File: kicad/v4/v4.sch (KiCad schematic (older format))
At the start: 31 parts, among them J1 BNC, J1-1 Head1_1, J1-2 Head1_1, J2 BNC, J2-1 Head1_1, J2-2 Head1_1, J2-3 Head1_1, J3 Red, J3-1 Head1_1, J3-2 Head1_1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

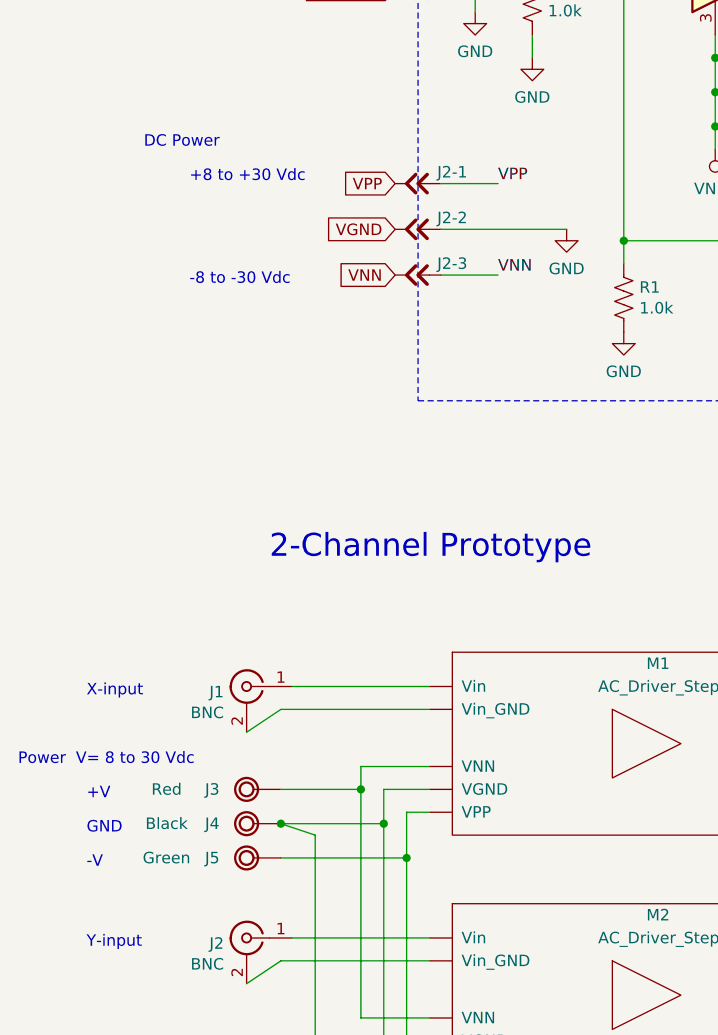
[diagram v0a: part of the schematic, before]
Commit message: Schematic:  Rename (reorder) power terminals to match the "as-built" board,     putting the negative supply first.
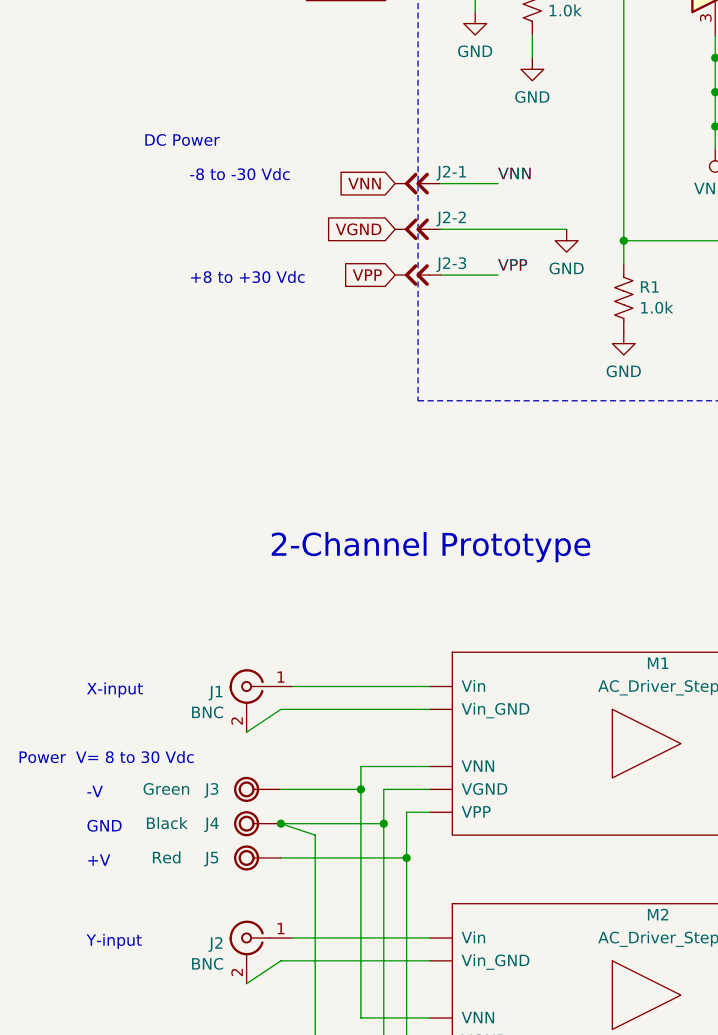
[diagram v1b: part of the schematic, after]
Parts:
- J3: value Red -> Green
- J5: value Green -> Red
- renumbered J2-3 to J2-1, J2-1 to J2-3
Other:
- moved on the sheet: J2-1, J2-3
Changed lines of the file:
@@
 Text Notes 7850 2900 0    50   ~ 0
 1:11.8
-Text GLabel 2200 3150 0    50   Input ~ 0
+Text GLabel 2200 3550 0    50   Input ~ 0
 VPP
 Text GLabel 2200 3350 0    50   Input ~ 0
 VGND
-Text GLabel 2200 3550 0    50   Input ~ 0
+Text GLabel 2200 3150 0    50   Input ~ 0
 VNN
+Text Notes 1300 3600 0    50   ~ 0
++8 to +30 Vdc
 Text Notes 1300 3150 0    50   ~ 0
-+8 to +30 Vdc
-Text Notes 1300 3600 0    50   ~ 0
 -8 to -30 Vdc
 $Comp
@@
 P 1550 5800
 F 0 "J3" H 1400 5800 50  0000 C CNN
-F 1 "Red" H 1200 5800 50  0000 C CNN
+F 1 "Green" H 1200 5800 50  0000 C CNN
 F 2 "" H 1550 5800 50  0001 C CNN
 F 3 "" H 1550 5800 50  0001 C CNN
@@
 P 1550 6100
 F 0 "J5" H 1400 6100 50  0000 C CNN
-F 1 "Green" H 1200 6100 50  0000 C CNN
+F 1 "Red" H 1200 6100 50  0000 C CNN
 F 2 "" H 1550 6100 50  0001 C CNN
 F 3 "" H 1550 6100 50  0001 C CNN
@@
 	2400 3350 2950 3350
 $Comp
+L _Local:Head1_1 J2-3
+U 1 1 5C40469D
+P 2300 3550
+F 0 "J2-3" H 2150 3600 50  0000 C CNN
+F 1 "Head1_1" H 2300 3350 50  0001 C CNN
+F 2 "" H 2300 3550 50  0001 C CNN
+F 3 "" H 2300 3550 50  0001 C CNN
+	1    2300 3550
+	-1   0    0    -1
+$EndComp
+$Comp
 L _Local:Head1_1 J2-1
-U 1 1 5C40469D
+U 1 1 5C4046F5
 P 2300 3150
 F 0 "J2-1" H 2150 3200 50  0000 C CNN
@@
 	-1   0    0    -1
 $EndComp
-$Comp
-L _Local:Head1_1 J2-3
-U 1 1 5C4046F5
-P 2300 3550
-F 0 "J2-3" H 2150 3600 50  0000 C CNN
-F 1 "Head1_1" H 2300 3350 50  0001 C CNN
-F 2 "" H 2300 3550 50  0001 C CNN
-F 3 "" H 2300 3550 50  0001 C CNN
-	1    2300 3550
-	-1   0    0    -1
-$EndComp
+Text Label 2650 3550 0    50   ~ 0
+VPP
+Wire Wire Line
+	2400 3550 2650 3550
+Wire Wire Line
+	2400 3150 2650 3150
 Text Label 2650 3150 0    50   ~ 0
-VPP
-Wire Wire Line
-	2400 3150 2650 3150
-Wire Wire Line
-	2400 3550 2650 3550
-Text Label 2650 3550 0    50   ~ 0
 VNN
 $Comp
@@
 Y-input
 Text Notes 850  5850 0    50   ~ 0
+-V
+Text Notes 850  6150 0    50   ~ 0
 +V
-Text Notes 850  6150 0    50   ~ 0
--V
 Text Notes 850  6000 0    50   ~ 0
 GND

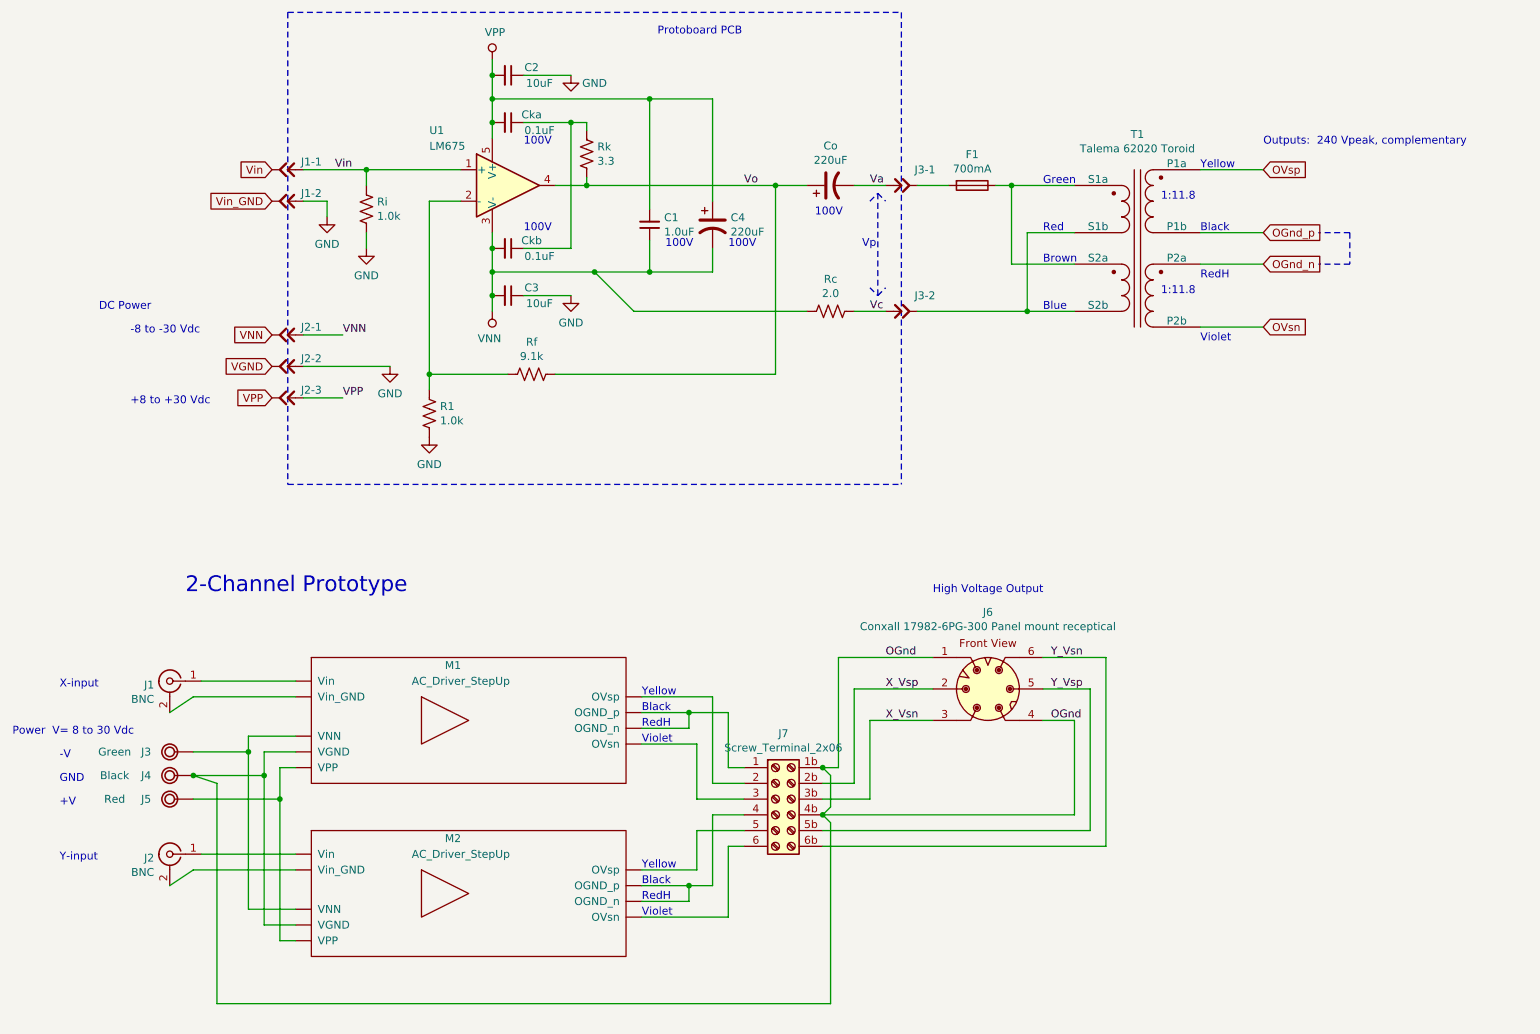
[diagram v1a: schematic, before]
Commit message: Schematic:  Add input/output notes and transformer rating.
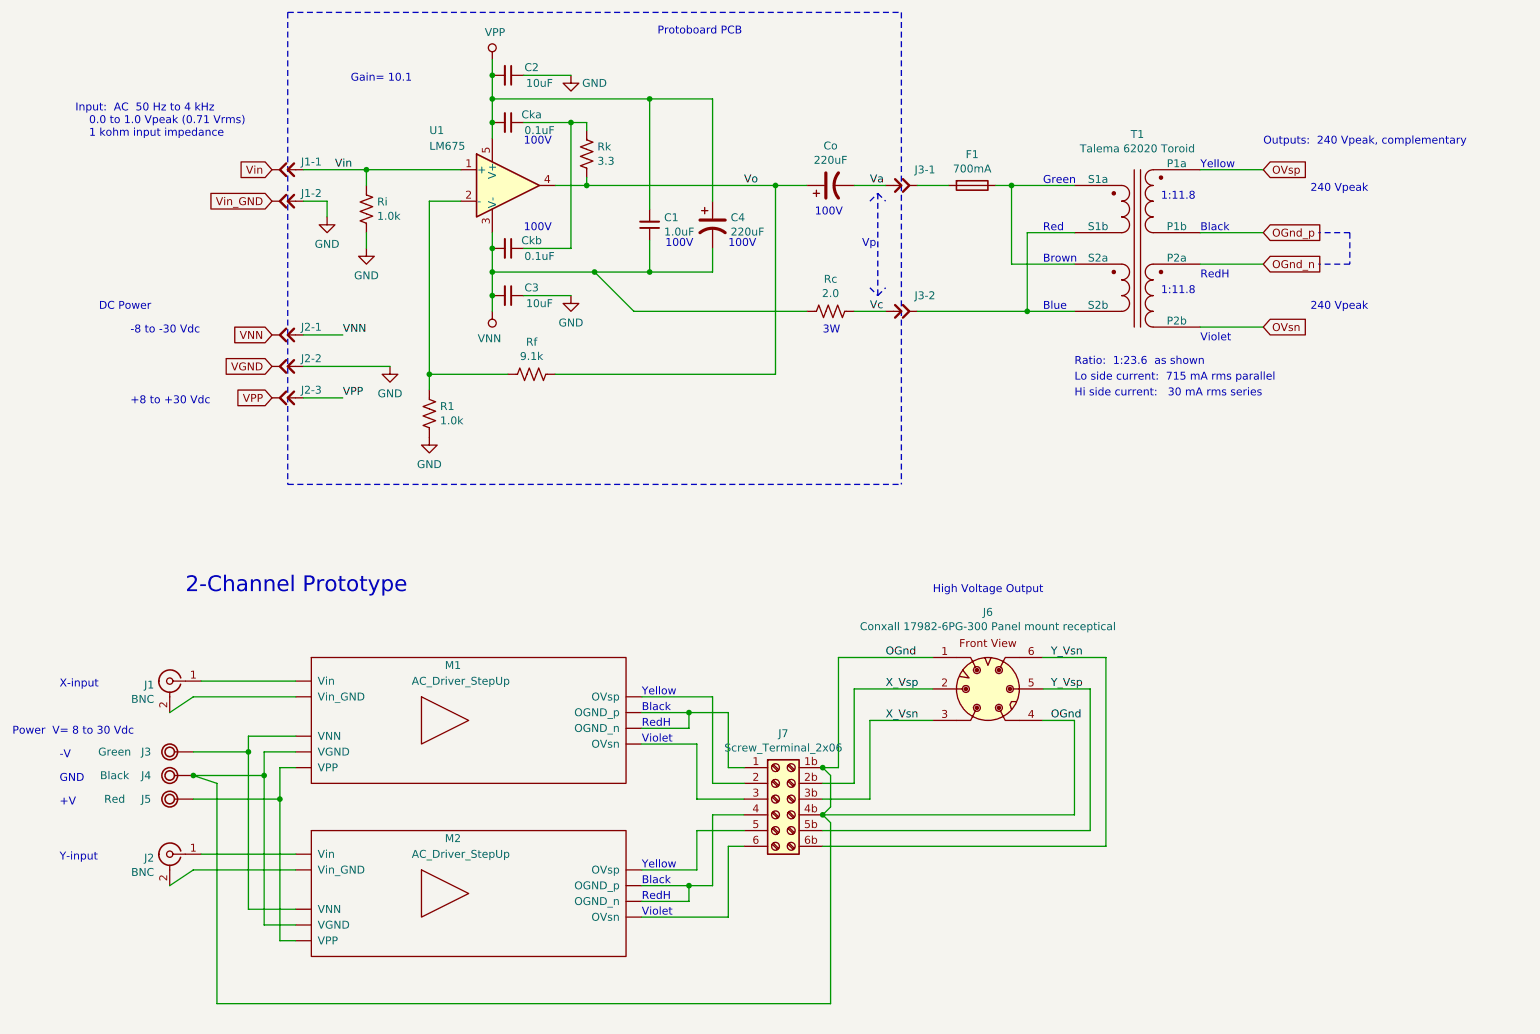
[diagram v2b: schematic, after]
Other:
- note added: "240 Vpeak"
- note added: "3W"
- note added: "Gain= 10.1"
- note added: "Hi side current: 30 mA rms series"
- note added: "Input: AC 50 Hz to 4 kHz\n 0.0 to 1.0 Vpeak (0.71 Vrms)\n 1 kohm input impedance"
- note added: "Lo side current: 715 mA rms parallel"
- note added: "Ratio: 1:23.6 as shown"
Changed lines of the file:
@@
 Sheet 1 1
 Title "Piezo AC Driver - v4, Protoboard"
-Date "2019-01-05"
+Date "2019-02-17"
 Rev ""
-Comp ""
+Comp "William A. Hudson"
 Comment1 ""
 Comment2 ""
@@
 Text Notes 3800 1950 0    50   ~ 0
 100V
+Text Notes 7300 3350 0    50   ~ 0
+Ratio:  1:23.6  as shown
+Text Notes 2700 1550 0    50   ~ 0
+Gain= 10.1
+Text Notes 950  1900 0    50   ~ 0
+Input:  AC  50 Hz to 4 kHz\n    0.0 to 1.0 Vpeak (0.71 Vrms)\n    1 kohm input impedance
+Text Notes 5700 3150 0    50   ~ 0
+3W
+Text Notes 7300 3450 0    50   ~ 0
+Lo side current:  715 mA rms parallel
+Text Notes 8800 2250 0    50   ~ 0
+240 Vpeak
+Text Notes 8800 3000 0    50   ~ 0
+240 Vpeak
+Text Notes 7300 3550 0    50   ~ 0
+Hi side current:   30 mA rms series
 $EndSCHEMATC

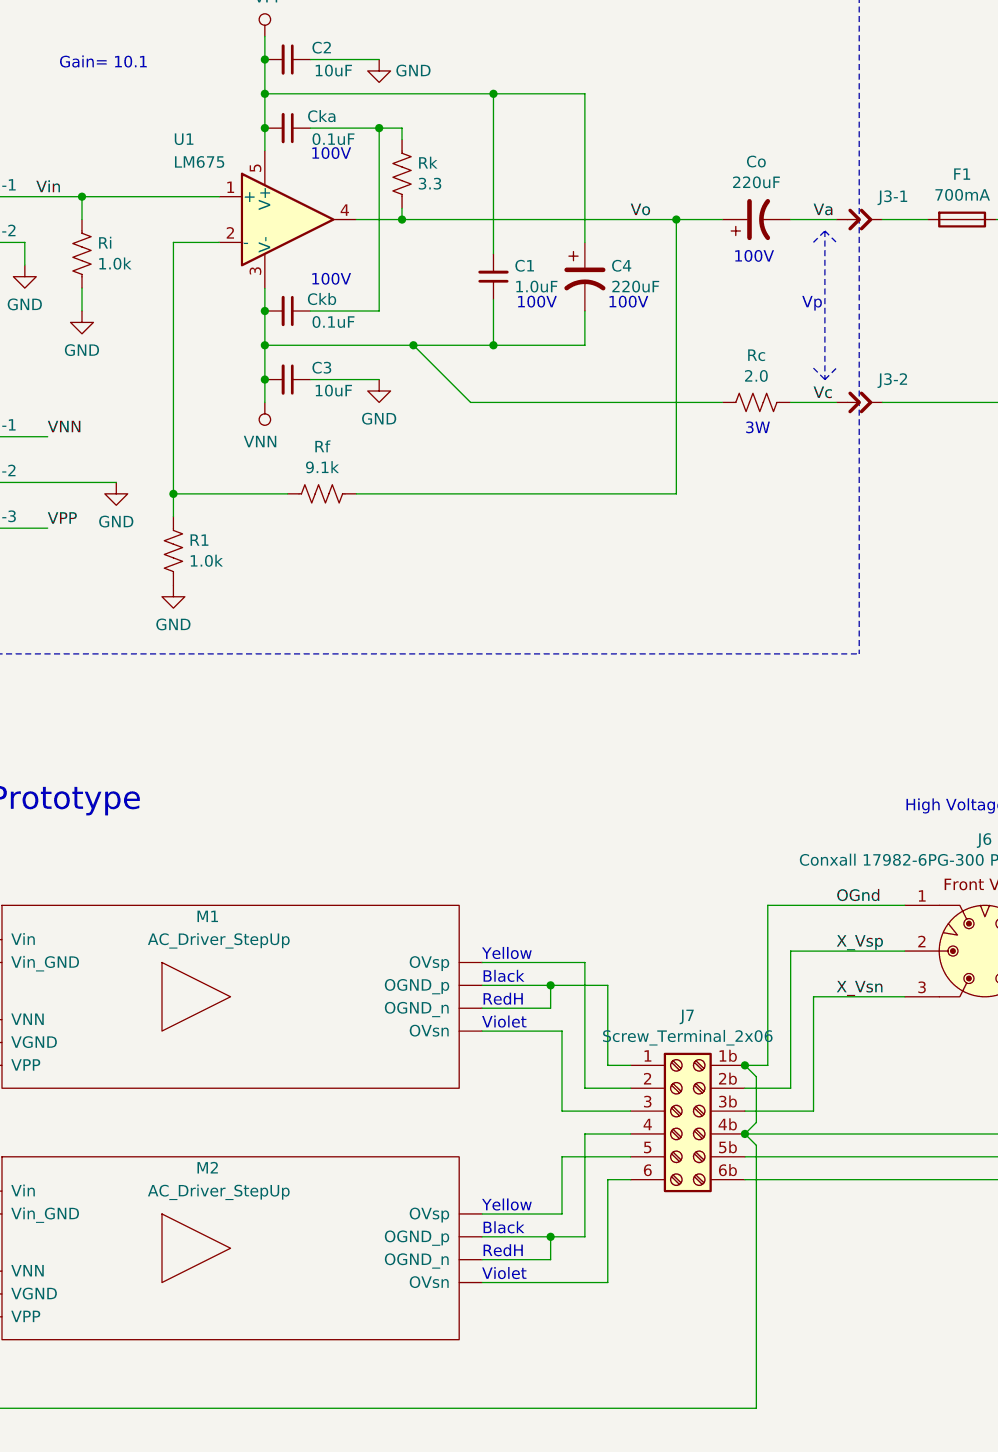
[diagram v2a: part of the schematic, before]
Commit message: Schematic:  Version v4b.  Add test points on op-amp output Vo and current     measuring resistor Vc.     Add PDF in Git, to help people looking at repository.
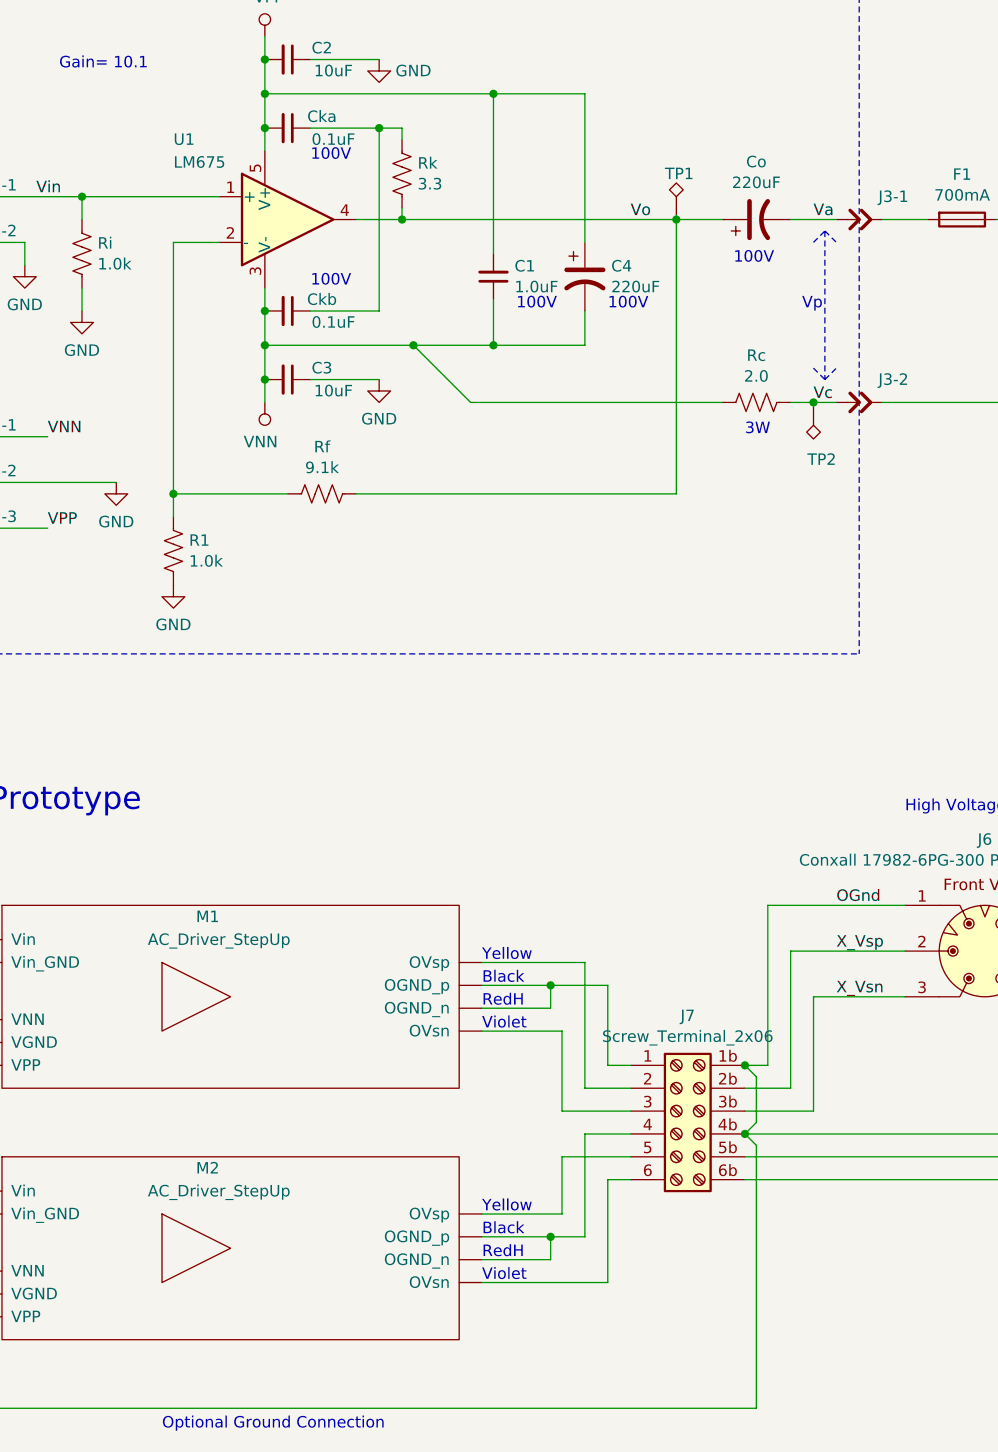
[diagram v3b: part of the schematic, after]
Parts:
- added TP1, TP2: TestPoint_Alt, symbol Connector:TestPoint_Alt
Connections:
- net Vc: now also TP2.1
- net Vo: now also TP1.1
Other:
- note added: "Optional Ground Connection"
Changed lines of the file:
@@
 encoding utf-8
 Sheet 1 1
-Title "Piezo AC Driver - v4, Protoboard"
-Date "2019-02-17"
+Title "Piezo AC Driver - v4b, Protoboard"
+Date "2019-03-27"
 Rev ""
 Comp "William A. Hudson"
@@
 	5900 2200 6100 2200
 Wire Wire Line
-	5900 3000 6100 3000
+	5900 3000 6000 3000
 Text Notes 1100 3000 0    50   ~ 0
 DC Power
@@
 Text Notes 7300 3550 0    50   ~ 0
 Hi side current:   30 mA rms series
+$Comp
+L Connector:TestPoint_Alt TP1
+U 1 1 5CA2AFDA
+P 5400 2200
+F 0 "TP1" H 5350 2400 50  0000 L CNN
+F 1 "TestPoint_Alt" H 5458 2229 50  0001 L CNN
+F 2 "" H 5600 2200 50  0001 C CNN
+F 3 "~" H 5600 2200 50  0001 C CNN
+	1    5400 2200
+	1    0    0    -1
+$EndComp
+$Comp
+L Connector:TestPoint_Alt TP2
+U 1 1 5CA2B247
+P 6000 3000
+F 0 "TP2" H 6100 3250 50  0000 R CNN
+F 1 "TestPoint_Alt" H 6058 3029 50  0001 L CNN
+F 2 "" H 6200 3000 50  0001 C CNN
+F 3 "~" H 6200 3000 50  0001 C CNN
+	1    6000 3000
+	1    0    0    1
+$EndComp
+Connection ~ 6000 3000
+Wire Wire Line
+	6000 3000 6100 3000
+Text Notes 3150 7500 0    50   ~ 0
+Optional Ground Connection
 $EndSCHEMATC
